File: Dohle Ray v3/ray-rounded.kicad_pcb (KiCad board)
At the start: 2 copper layers, 50 x 91.5 mm, 33 parts, among them J1 Conn_01x07_Female, J2 AudioJack3, J3 AudioJack3, Q1 J201, SW1 3pdt_footswitch, U1 TL082

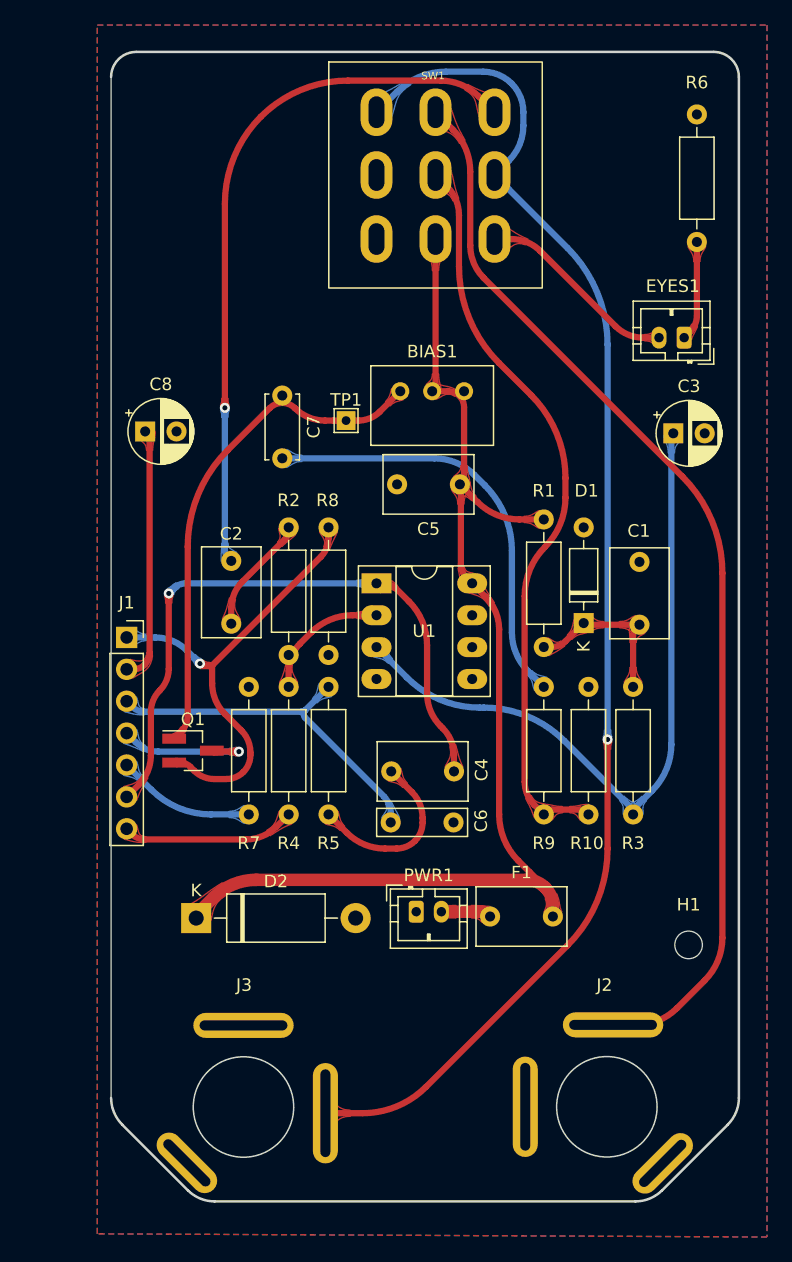
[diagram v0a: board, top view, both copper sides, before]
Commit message: Update version and fix faulty jack wiring
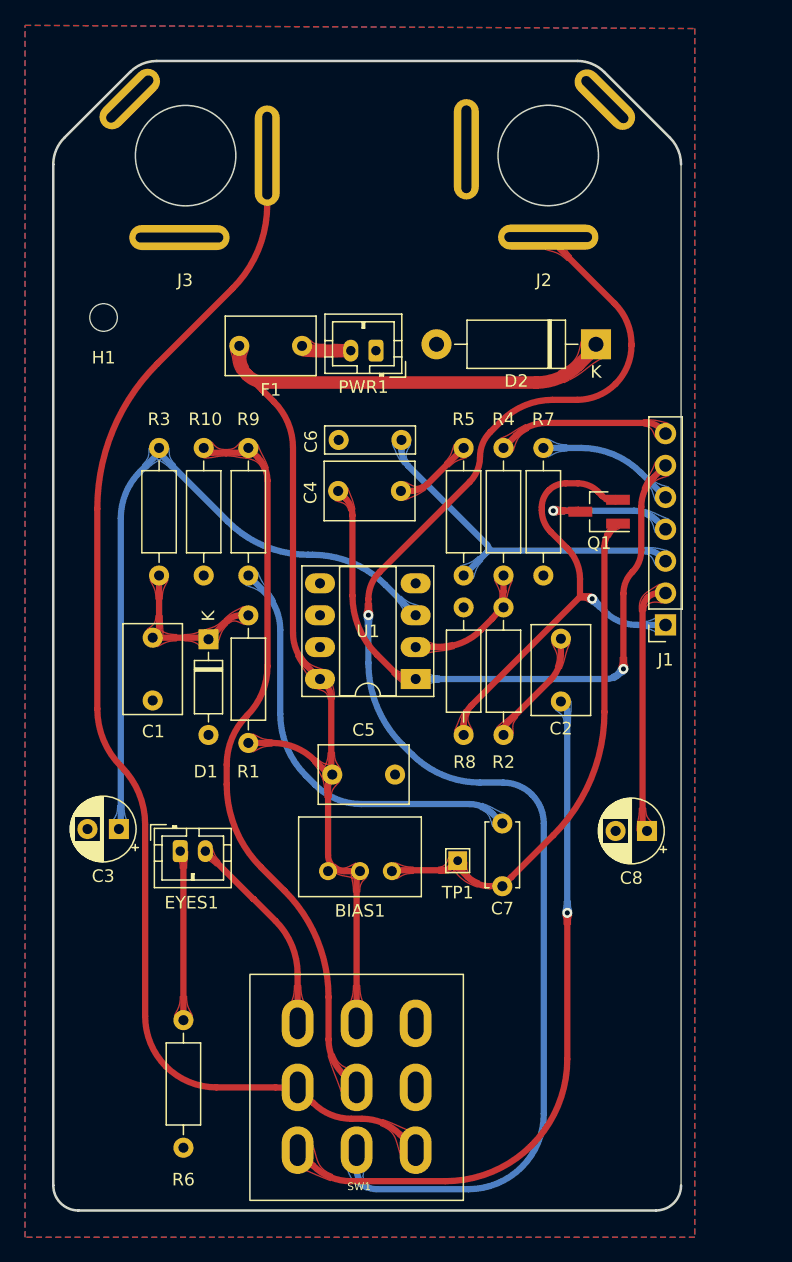
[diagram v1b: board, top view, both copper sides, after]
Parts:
- moved J2 86.6 mm to (134.4, 58.7), turned to 180 degrees
- moved J3 86.6 mm to (96.0, 69.4), turned to -90 degrees
- moved R6 74.3 mm to (105.9, 137.7), turned to -90 degrees
- moved SW1 73.1 mm to (119.0, 143.0), turned to 180 degrees
- moved H1 68.3 mm to (99.6, 81.7), turned to 180 degrees
- moved EYES1 57.3 mm to (105.7, 124.2), turned to 0 degrees
- moved D2 55.7 mm to (138.8, 83.8), turned to 180 degrees
- moved C3 54.2 mm to (100.8, 122.4), turned to 180 degrees
- moved C8 51.1 mm to (142.8, 122.6), turned to 180 degrees
- moved F1 47.8 mm to (115.4, 84.0), turned to 180 degrees
- moved PWR1 44.8 mm to (121.2, 84.3), turned to 180 degrees
- moved J1 42.9 mm to (144.3, 106.2), turned to 180 degrees
- moved C7 42.8 mm to (131.3, 127.0), turned to 90 degrees
- moved C1 40.3 mm to (103.5, 112.2), turned to 90 degrees
- moved BIAS1 39.7 mm to (117.4, 125.8), turned to 180 degrees
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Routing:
- net Net-(J2-PadT): track 86.6 -> 112.4 mm, vias 0 -> 1
- net Net-(J3-PadT): track 109.4 -> 100.0 mm, vias 1 -> 0
- net Net-(C4-Pad2): track 14.5 -> 6.32 mm
- net Net-(EYES1-Pad1): track 7.96 -> 13.5 mm
- net Net-(BIAS1-Pad3): track 40.5 -> 41.6 mm
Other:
- board size 50 x 91.5 mm -> 50 x 91.6 mm
- board text added: "Dohle Ray v3.1a"
- board text added: "Published under CC BY-NC-SA 3.0 license"
- board text removed: "Dohle Ray v3.0a"

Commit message: Update resistor values to have unity gain at 0% volume and gain knob, update PCB revision
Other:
- board text added: "Dohle Ray v3.1"
- board text removed: "Dohle Ray v3.1a"
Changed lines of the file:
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@@
       (xy 103.147567 144.703117)
     ) (layer "B.SilkS") (width 0.034835) (fill solid))
-  (gr_line (start 109.833016 132.77358) (end 109.833016 131.75758) (layer "B.Mask") (width 0.25))
-  (gr_line (start 110.348594 132.265214) (end 109.332594 132.265214) (layer "B.Mask") (width 0.25))
-  (gr_rect (start 110.819121 133.270739) (end 108.863321 131.289539) (layer "B.Mask") (width 0.25) (fill none))
+  (gr_line (start 109.449683 132.77358) (end 109.449683 131.75758) (layer "B.Mask") (width 0.25))
+  (gr_line (start 109.965261 132.265214) (end 108.949261 132.265214) (layer "B.Mask") (width 0.25))
+  (gr_rect (start 110.435788 133.270739) (end 108.479988 131.289539) (layer "B.Mask") (width 0.25) (fill none))
   (gr_line (start 113.152141 134.009276) (end 113.152141 133.509276) (layer "Dwgs.User") (width 0.2))
   (gr_line (start 124.052141 152.009276) (end 126.252141 152.009276) (layer "Dwgs.User") (width 0.2))
@@
     (effects (font (size 1.5 1.5) (thickness 0.2)) (justify mirror))
   )
-  (gr_text "Made in Switzerland" (at 121.668333 132.255387) (layer "B.Mask")
+  (gr_text "Made in Switzerland" (at 121.285 132.255387) (layer "B.Mask")
     (effects (font (size 1.3 1.3) (thickness 0.25)) (justify mirror))
   )
-  (gr_text "Dohle Ray v3.1a\n" (at 119.4212 129.3568) (layer "B.Mask")
+  (gr_text "Dohle Ray v3.1\n" (at 119.4212 129.3568) (layer "B.Mask")
     (effects (font (size 1.3 1.3) (thickness 0.25)) (justify mirror))
   )
